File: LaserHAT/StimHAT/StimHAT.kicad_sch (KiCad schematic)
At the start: 120 parts, among them J1 GPIO, J10 OLED 0.91 (GND VCC SCL SDA), J101 ELECTRODE E1/E2, J102 B4B-PH-K-S(LF)(SN), J5 GT-USB-7010ASV, J6 BNC TRIGGER IN, J7 BNC STIM OUT, Q101 MMBT3904, Q102 MMBT3906, Q3 AP30P30Q, Q4 DMMT5401, Q5 AP30P30Q, SW10 MSK12C02, SW6 TS-1088-AR02016, SW7 SKRHADE010, SW9 TS-1088-AR02016, U1 M24C32-WDW6TP, U101 ISO7741FDBQR, U104 TLV76050DBZR, U105 DAC60501ZDGSR, U106 OPA2192IDGKR, U107 CD74HC4053PWR, U108 DG418DY-T1-E3, U109 ISO1640BDR, U110 TLV1702AIDGKR, U4 MCP1700T-3302E/MB, U5 AP2171W, U6 CH340N, U7 MSPM0G3507SRHBR, U8 74LVC2G17GW

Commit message: StimHAT: schematic audit fixes (VREFIO 1 uF, -4.3 V Zener for the 4053's supply margin, 250 mA 0805 inductor code, R113 0603); narrower net classes for routing
Co-Authored-By: Claude Fable 5.1 <noreply@anthropic.com>
Claude-Session: https://claude.ai/code/session_015kiXLxnPpBaXdXJu2EMvn7
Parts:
- C114: value 100nF -> 1uF; LCSC Part # C307331 -> C52923
- D102: value BZT52C4V7S -> BZT52C4V3S; LCSC Part # C353517 -> C22399888
- L101, L102: LCSC Part # C95978 -> C139245
- R113: footprint Resistor_SMD:R_0402_1005Metric -> Resistor_SMD:R_0603_1608Metric; LCSC Part # C25900 -> C23162
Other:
- note added: "(DG418 on, electrode shorted), high -> low. Signals stay within +/-1.25 V; the 4053 runs on +5 / -4.3 V (<= 9.7 V worst case of its 10 V recommended maximum)."
- note added: "clamp each rail to 20 V against GND_ISO (ICs are rated 25 V to their ground). U104: +5V_ISO. R113 / D102: -4.3 V for the 74HC4053."
- note removed: "(DG418 on, electrode shorted), high -> low. Signals stay within +/-1.25 V; the 4053 runs on +5 / -4.7 V (9.7 V of its 10.5 V maximum)."
- note removed: "clamp each rail to 20 V against GND_ISO (ICs are rated 25 V to their ground). U104: +5V_ISO. R113 / D102: -4.7 V for the 74HC4053."
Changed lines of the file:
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@@
     (property "Footprint" "Inductor_SMD:L_0805_2012Metric" (at 238.76 177.8 0) (effects (font (size 1.27 1.27)) (hide yes)))
     (property "Datasheet" "" (at 238.76 177.8 0) (effects (font (size 1.27 1.27)) (hide yes)))
-    (property "LCSC Part #" "C95978" (at 238.76 177.8 0) (effects (font (size 1.27 1.27)) (hide yes)))
+    (property "LCSC Part #" "C139245" (at 238.76 177.8 0) (effects (font (size 1.27 1.27)) (hide yes)))
     (pin "1")
     (pin "2")
@@
     (property "Footprint" "Inductor_SMD:L_0805_2012Metric" (at 238.76 254 0) (effects (font (size 1.27 1.27)) (hide yes)))
     (property "Datasheet" "" (at 238.76 254 0) (effects (font (size 1.27 1.27)) (hide yes)))
-    (property "LCSC Part #" "C95978" (at 238.76 254 0) (effects (font (size 1.27 1.27)) (hide yes)))
+    (property "LCSC Part #" "C139245" (at 238.76 254 0) (effects (font (size 1.27 1.27)) (hide yes)))
     (pin "1")
     (pin "2")
@@
     (property "Reference" "R113" (at 246.38 267.97  0) (effects (font (size 1.27 1.27)) (justify left)))
     (property "Value" "4.7k" (at 246.38 270.51  0) (effects (font (size 1.27 1.27)) (justify left)))
-    (property "Footprint" "Resistor_SMD:R_0402_1005Metric" (at 243.84 269.24 0) (effects (font (size 1.27 1.27)) (hide yes)))
+    (property "Footprint" "Resistor_SMD:R_0603_1608Metric" (at 243.84 269.24 0) (effects (font (size 1.27 1.27)) (hide yes)))
     (property "Datasheet" "" (at 243.84 269.24 0) (effects (font (size 1.27 1.27)) (hide yes)))
-    (property "LCSC Part #" "C25900" (at 243.84 269.24 0) (effects (font (size 1.27 1.27)) (hide yes)))
+    (property "LCSC Part #" "C23162" (at 243.84 269.24 0) (effects (font (size 1.27 1.27)) (hide yes)))
     (pin "1")
     (pin "2")
@@
   (symbol (lib_id "stimhat:D_Zener") (at 259.08 269.24 90) (unit 1) (exclude_from_sim no) (in_bom yes) (on_board yes) (dnp no)
     (property "Reference" "D102" (at 261.62 267.97  90) (effects (font (size 1.27 1.27)) (justify left)))
-    (property "Value" "BZT52C4V7S" (at 261.62 270.51  90) (effects (font (size 1.27 1.27)) (justify left)))
+    (property "Value" "BZT52C4V3S" (at 261.62 270.51  90) (effects (font (size 1.27 1.27)) (justify left)))
     (property "Footprint" "Diode_SMD:D_SOD-323" (at 259.08 269.24 0) (effects (font (size 1.27 1.27)) (hide yes)))
     (property "Datasheet" "" (at 259.08 269.24 0) (effects (font (size 1.27 1.27)) (hide yes)))
-    (property "LCSC Part #" "C353517" (at 259.08 269.24 0) (effects (font (size 1.27 1.27)) (hide yes)))
+    (property "LCSC Part #" "C22399888" (at 259.08 269.24 0) (effects (font (size 1.27 1.27)) (hide yes)))
     (pin "1")
     (pin "2")
@@
   (text "PS1 (hand-fitted) makes +/-15 V from the HAT's 5 V, or J102 brings +/-12..16.8 V from the battery pack (pin 4 = pin 2 = GND_ISO:" (exclude_from_sim no) (at 160.02 276.86 0) (effects (font (size 1.27 1.27)) (justify left bottom)))
   (text "the pack's plug interlock).  L / C filter, then Q101 / Q102 (base 4.7k / 10 uF: ~1.2 V drop, 60 dB ripple rejection above 100 Hz).  D103 / D104" (exclude_from_sim no) (at 160.02 281.94 0) (effects (font (size 1.27 1.27)) (justify left bottom)))
-  (text "clamp each rail to 20 V against GND_ISO (ICs are rated 25 V to their ground).  U104: +5V_ISO.  R113 / D102: -4.7 V for the 74HC4053." (exclude_from_sim no) (at 284.48 172.72 0) (effects (font (size 1.27 1.27)) (justify left bottom)))
+  (text "clamp each rail to 20 V against GND_ISO (ICs are rated 25 V to their ground).  U104: +5V_ISO.  R113 / D102: -4.3 V for the 74HC4053." (exclude_from_sim no) (at 284.48 172.72 0) (effects (font (size 1.27 1.27)) (justify left bottom)))
   (rectangle (start 15.24 289.56) (end 241.3 416.56) (stroke (width 0.2) (type dash)) (fill (type none)))
   (text "6. SET-POINT: DAC60501 (I2C 0x48, 0..1.25 V = VSET_P), U106B INVERTS -> VSET_N, 74HC4053 PICKS SIGN (CATH) AND GATES (EN)" (exclude_from_sim no) (at 16.51 293.37 0) (effects (font (size 2.0 2.0) (bold yes)) (justify left bottom)))
@@
   (symbol (lib_id "stimhat:C") (at 81.28 345.44 0) (unit 1) (exclude_from_sim no) (in_bom yes) (on_board yes) (dnp no)
     (property "Reference" "C114" (at 83.82 344.17  0) (effects (font (size 1.27 1.27)) (justify left)))
-    (property "Value" "100nF" (at 83.82 346.71  0) (effects (font (size 1.27 1.27)) (justify left)))
+    (property "Value" "1uF" (at 83.82 346.71  0) (effects (font (size 1.27 1.27)) (justify left)))
     (property "Footprint" "Capacitor_SMD:C_0402_1005Metric" (at 81.28 345.44 0) (effects (font (size 1.27 1.27)) (hide yes)))
     (property "Datasheet" "" (at 81.28 345.44 0) (effects (font (size 1.27 1.27)) (hide yes)))
-    (property "LCSC Part #" "C307331" (at 81.28 345.44 0) (effects (font (size 1.27 1.27)) (hide yes)))
+    (property "LCSC Part #" "C52923" (at 81.28 345.44 0) (effects (font (size 1.27 1.27)) (hide yes)))
     (pin "1")
     (pin "2")
@@
   )
   (text "Switch 1: CATH picks VSET_P (0) / VSET_N (1) -> SW_P.  Switch 2: EN picks 0 V (0) / SW_P (1) -> V_IN.  Switch 3: RELEASE low -> SHORT_IN high" (exclude_from_sim no) (at 17.78 403.86 0) (effects (font (size 1.27 1.27)) (justify left bottom)))
-  (text "(DG418 on, electrode shorted), high -> low.  Signals stay within +/-1.25 V; the 4053 runs on +5 / -4.7 V (9.7 V of its 10.5 V maximum)." (exclude_from_sim no) (at 17.78 408.94 0) (effects (font (size 1.27 1.27)) (justify left bottom)))
+  (text "(DG418 on, electrode shorted), high -> low.  Signals stay within +/-1.25 V; the 4053 runs on +5 / -4.3 V (<= 9.7 V worst case of its 10 V recommended maximum)." (exclude_from_sim no) (at 17.78 408.94 0) (effects (font (size 1.27 1.27)) (justify left bottom)))
   (text "DAC60501Z: write GAIN (0x04) = 0x0100 first, then DAC (0x08) = code << 4; readback over the same bus.  C115 at U105 VDD, C118 / C119 at U107." (exclude_from_sim no) (at 17.78 414.02 0) (effects (font (size 1.27 1.27)) (justify left bottom)))
   (rectangle (start 248.92 289.56) (end 347.98 391.16) (stroke (width 0.2) (type dash)) (fill (type none)))

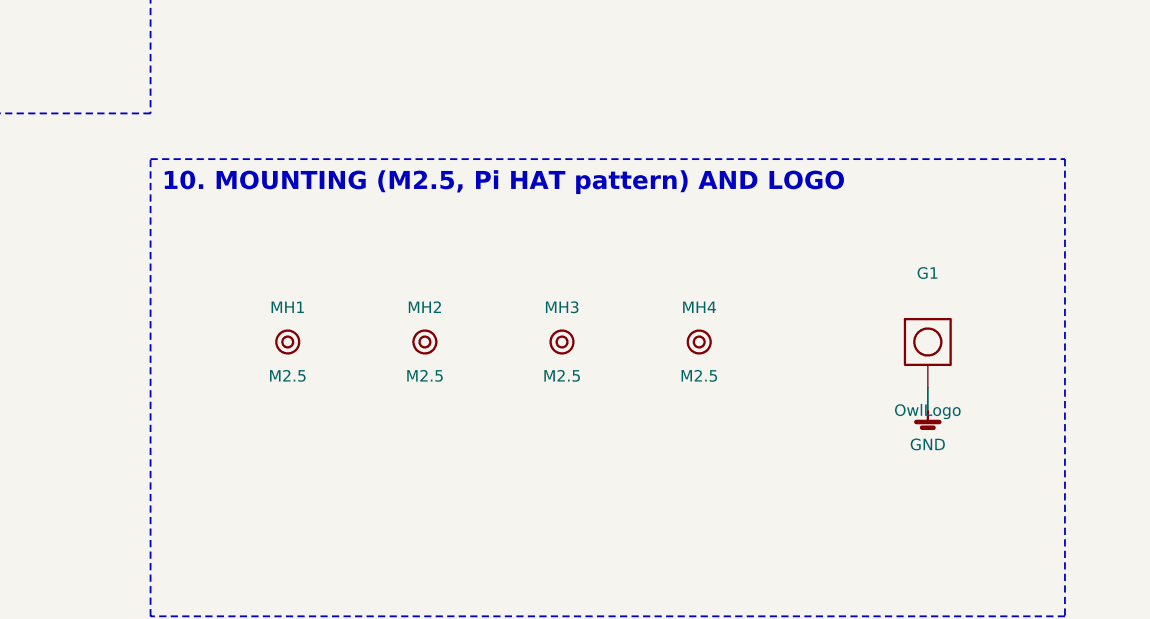
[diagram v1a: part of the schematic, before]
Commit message: StimHAT rev A: routed board (Freerouting + fan-out + SDA_H pre-route), DRC 0/0, fab outputs
Board: placement per floorplan 1g, 2.5 mm isolation barrier as rule areas + .kicad_dru, routed by
tools/autoroute.py (rip -> tools/fanout.py dog-bone fan-out of U7/U101 + GND thermal vias in U7's pad ->
tools/preroute.py locked SDA_H -> Freerouting 500 passes -> trim unused fan-out vias); 0 DRC errors,
0 unconnected, ERC 0/0, path_check and sync_check clean.  Silk of the edge-overhanging connectors
(J6, J7, J101, PS1) stripped from the board copies; joystick footprint loses its silk circle; logo dropped.
fab/StimHAT: gerbers, JLC BOM/CPL, renders.  tools/fixups.py: track/via/silk-strip/maze helpers.

Co-Authored-By: Claude Fable 5.1 <noreply@anthropic.com>
Claude-Session: https://claude.ai/code/session_015kiXLxnPpBaXdXJu2EMvn7
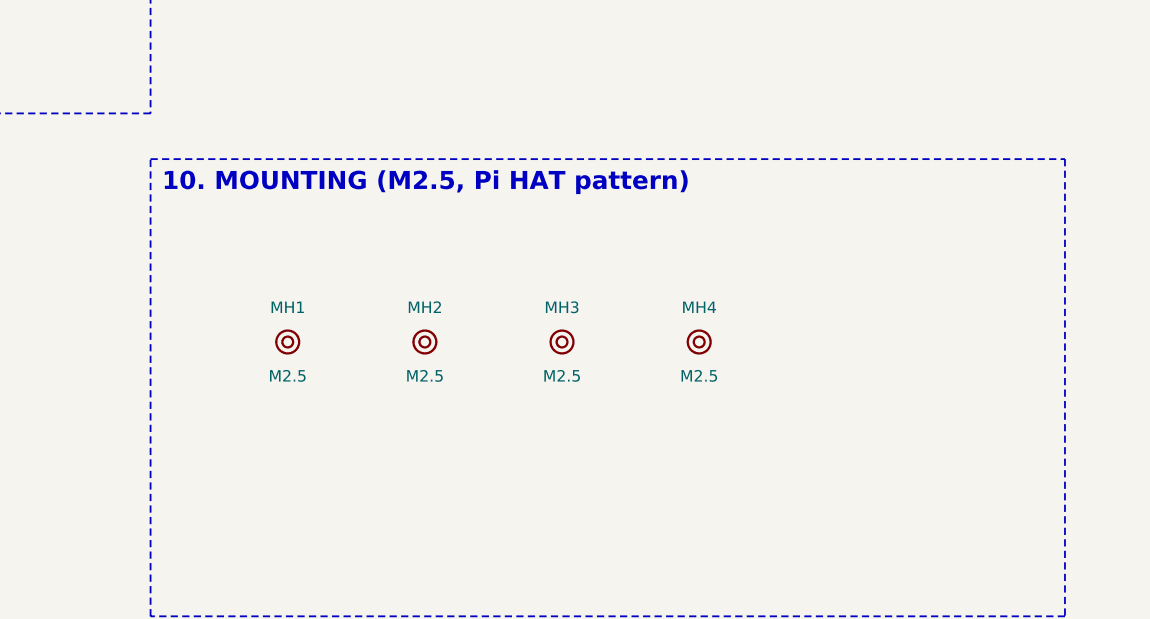
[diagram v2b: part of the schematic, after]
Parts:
- removed G1: OwlLogo, Footprints:OwlLogo_Laser_14mm, symbol stimhat:Logo
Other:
- note added: "10. MOUNTING (M2.5, Pi HAT pattern)"
- note removed: "10. MOUNTING (M2.5, Pi HAT pattern) AND LOGO"
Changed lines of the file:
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@@
   (text "while +5V_ISO is down and when one rail is missing.  R120 / D101 shift the -V-referenced open collectors to 0..5 V." (exclude_from_sim no) (at 358.14 393.7 0) (effects (font (size 1.27 1.27)) (justify left bottom)))
   (rectangle (start 508 162.56) (end 609.6 213.36) (stroke (width 0.2) (type dash)) (fill (type none)))
-  (text "10. MOUNTING (M2.5, Pi HAT pattern) AND LOGO" (exclude_from_sim no) (at 509.27 166.37 0) (effects (font (size 2.0 2.0) (bold yes)) (justify left bottom)))
+  (text "10. MOUNTING (M2.5, Pi HAT pattern)" (exclude_from_sim no) (at 509.27 166.37 0) (effects (font (size 2.0 2.0) (bold yes)) (justify left bottom)))
   (symbol (lib_id "stimhat:MountingHole") (at 523.24 182.88 0) (unit 1) (exclude_from_sim no) (in_bom no) (on_board yes) (dnp no)
     (property "Reference" "MH1" (at 523.24 179.07  0) (effects (font (size 1.27 1.27)) ))
@@
     (property "Datasheet" "" (at 568.96 182.88 0) (effects (font (size 1.27 1.27)) (hide yes)))
     (instances (project "StimHAT" (path "/15556796-a1bc-5b7f-a5a5-0a862d310368" (reference "MH4") (unit 1))))
-  )
-  (symbol (lib_id "stimhat:Logo") (at 594.36 182.88 0) (unit 1) (exclude_from_sim no) (in_bom no) (on_board yes) (dnp no)
-    (property "Reference" "G1" (at 594.36 175.26  0) (effects (font (size 1.27 1.27)) ))
-    (property "Value" "OwlLogo" (at 594.36 190.5  0) (effects (font (size 1.27 1.27)) ))
-    (property "Footprint" "Footprints:OwlLogo_Laser_14mm" (at 594.36 182.88 0) (effects (font (size 1.27 1.27)) (hide yes)))
-    (property "Datasheet" "" (at 594.36 182.88 0) (effects (font (size 1.27 1.27)) (hide yes)))
-    (pin "1")
-    (instances (project "StimHAT" (path "/15556796-a1bc-5b7f-a5a5-0a862d310368" (reference "G1") (unit 1))))
-  )
-  (symbol (lib_id "stimhat:GND") (at 594.36 190.5 0) (unit 1) (exclude_from_sim no) (in_bom no) (on_board no) (dnp no)
-    (property "Reference" "#PWR195" (at 594.36 190.5 0) (effects (font (size 1.27 1.27)) (hide yes)))
-    (property "Value" "GND" (at 594.36 194.31 0) (effects (font (size 1.27 1.27))))
-    (property "Footprint" "" (at 594.36 190.5 0) (effects (font (size 1.27 1.27)) (hide yes)))
-    (property "Datasheet" "" (at 594.36 190.5 0) (effects (font (size 1.27 1.27)) (hide yes)))
-    (pin "1")
-    (instances (project "StimHAT" (path "/15556796-a1bc-5b7f-a5a5-0a862d310368" (reference "#PWR195") (unit 1))))
   )
   (no_connect (at 38.1 68.58))
@@
   (wire (pts (xy 447.04 313.69) (xy 447.04 316.23)) (stroke (width 0) (type default)))
   (wire (pts (xy 482.6 375.92) (xy 482.6 378.46)) (stroke (width 0) (type default)))
-  (wire (pts (xy 594.36 187.96) (xy 594.36 190.5)) (stroke (width 0) (type default)))
   (junction (at 33.02 60.96) (diameter 0) (color 0 0 0 0))
   (junction (at 68.58 60.96) (diameter 0) (color 0 0 0 0))

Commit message: StimHAT rev A: audit fixes (schematic + layout), isolation rule proven live, board finished by hand
Schematic (independent review): CH340N on MSPM0_3V3 (no back-feed into the unpowered MCU), C17 at U6, C18 at
U1, R3 10k, R19/R20 DNP, C125/C126 at the DG418, VREFIO/OA_IN/U5B_IN/OA_OUT labelled, in_bom flags match the
board.  Layout (independent review): the .kicad_dru rules were silently ignored because of their (comment ...)
entries - comments removed, liveness proven with a 25 mm test; three real barrier intrusions fixed (I2C loop above
U109, passage vs strip B pads); standoff keep-outs exclude tracks; decouplers next to their pins; Rails class;
the 0.3 mm +/- rail rule dropped (0.15 class, IPC-2221 B4).  Routing: fan-out + pre-routes (tab, passage, SDA_H)
then Freerouting, the last connections and all DRC fixes by hand (tools/fixups.py).  DRC 0 errors / 0 unconnected,
ERC 0/0, path/sync checks clean; fab outputs regenerated.

Co-Authored-By: Claude Fable 5.1 <noreply@anthropic.com>
Claude-Session: https://claude.ai/code/session_015kiXLxnPpBaXdXJu2EMvn7
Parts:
- added C125, C126: 100nF 50V, Capacitor_SMD:C_0603_1608Metric, symbol stimhat:C
- added C17, C18: 100nF, Capacitor_SMD:C_0402_1005Metric, symbol stimhat:C
- J1, J10, J101, J102, J6, J7, JP1, JP4, JP5, PS1: now left out of the parts list
- R19, R20: now not fitted
- R3: value 47k -> 10k; LCSC Part # C25792 -> C25744
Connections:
- net +3V3: no longer U6.5 (VCC), U6.8 (V3)
- net +3V3_PI: now also C18.1
- net +V_STIM: now also C125.1
- net -V_STIM: now also C126.2
- net GND: now also C17.2, C18.2
- net GND_ISO: now also C125.2, C126.1
- net MSPM0_3V3: now also U6.5 (VCC), U6.8 (V3), C17.1
- net U5B_IN: now reaches R105.2, R106.1, U106.6 (-)
- net OA_OUT: now reaches R115.1, U106.1
- net OA_IN: now reaches C120.1, R114.2, U106.3 (+)
- net VREFIO: now reaches C114.1, U105.10 (VREFIO)

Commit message: StimHAT: second schematic review (no blocker/major): R1/R2 fitted per the HAT guide, R107/R108 2.2k, stale texts, notes
Co-Authored-By: Claude Fable 5.1 <noreply@anthropic.com>
Claude-Session: https://claude.ai/code/session_015kiXLxnPpBaXdXJu2EMvn7
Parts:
- R1, R2: now fitted
- R107, R108: value 4.7k -> 2.2k; LCSC Part # C25900 -> C25879
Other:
- note added: "5. ISOLATED POWER: A0515S (PS1) OR THE BATTERY PACK (J102), LC + CAPACITANCE MULTIPLIERS, CLAMPS, +5 / -4.3 V"
- note added: "Taps at 0.043 x (V+ + |V-|) inside each rail (1.15 V at +/-13.5 V). FAULT_n low while |E1| is past the trip point,"
- note removed: "5. ISOLATED POWER: A0515S (PS1) OR THE BATTERY PACK (J102), LC + CAPACITANCE MULTIPLIERS, CLAMPS, +5 / -4.7 V"
- note removed: "Taps at 0.043 x (V+ + |V-|) inside each rail (0.9 V at +/-13.5 V). FAULT_n low while |E1| is past the trip point,"
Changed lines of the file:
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@@
     (instances (project "StimHAT" (path "/15556796-a1bc-5b7f-a5a5-0a862d310368" (reference "#PWR052") (unit 1))))
   )
-  (symbol (lib_id "stimhat:R") (at 238.76 121.92 0) (unit 1) (exclude_from_sim no) (in_bom yes) (on_board yes) (dnp yes)
+  (symbol (lib_id "stimhat:R") (at 238.76 121.92 0) (unit 1) (exclude_from_sim no) (in_bom yes) (on_board yes) (dnp no)
     (property "Reference" "R1" (at 241.3 120.65  0) (effects (font (size 1.27 1.27)) (justify left)))
     (property "Value" "3.9k" (at 241.3 123.19  0) (effects (font (size 1.27 1.27)) (justify left)))
@@
     (instances (project "StimHAT" (path "/15556796-a1bc-5b7f-a5a5-0a862d310368" (reference "R1") (unit 1))))
   )
-  (symbol (lib_id "stimhat:R") (at 248.92 121.92 0) (unit 1) (exclude_from_sim no) (in_bom yes) (on_board yes) (dnp yes)
+  (symbol (lib_id "stimhat:R") (at 248.92 121.92 0) (unit 1) (exclude_from_sim no) (in_bom yes) (on_board yes) (dnp no)
     (property "Reference" "R2" (at 251.46 120.65  0) (effects (font (size 1.27 1.27)) (justify left)))
     (property "Value" "3.9k" (at 251.46 123.19  0) (effects (font (size 1.27 1.27)) (justify left)))
@@
   (symbol (lib_id "stimhat:R") (at 25.4 213.36 0) (unit 1) (exclude_from_sim no) (in_bom yes) (on_board yes) (dnp no)
     (property "Reference" "R107" (at 27.94 212.09  0) (effects (font (size 1.27 1.27)) (justify left)))
-    (property "Value" "4.7k" (at 27.94 214.63  0) (effects (font (size 1.27 1.27)) (justify left)))
+    (property "Value" "2.2k" (at 27.94 214.63  0) (effects (font (size 1.27 1.27)) (justify left)))
     (property "Footprint" "Resistor_SMD:R_0402_1005Metric" (at 25.4 213.36 0) (effects (font (size 1.27 1.27)) (hide yes)))
     (property "Datasheet" "" (at 25.4 213.36 0) (effects (font (size 1.27 1.27)) (hide yes)))
-    (property "LCSC Part #" "C25900" (at 25.4 213.36 0) (effects (font (size 1.27 1.27)) (hide yes)))
+    (property "LCSC Part #" "C25879" (at 25.4 213.36 0) (effects (font (size 1.27 1.27)) (hide yes)))
     (pin "1")
     (pin "2")
@@
   (symbol (lib_id "stimhat:R") (at 35.56 213.36 0) (unit 1) (exclude_from_sim no) (in_bom yes) (on_board yes) (dnp no)
     (property "Reference" "R108" (at 38.1 212.09  0) (effects (font (size 1.27 1.27)) (justify left)))
-    (property "Value" "4.7k" (at 38.1 214.63  0) (effects (font (size 1.27 1.27)) (justify left)))
+    (property "Value" "2.2k" (at 38.1 214.63  0) (effects (font (size 1.27 1.27)) (justify left)))
     (property "Footprint" "Resistor_SMD:R_0402_1005Metric" (at 35.56 213.36 0) (effects (font (size 1.27 1.27)) (hide yes)))
     (property "Datasheet" "" (at 35.56 213.36 0) (effects (font (size 1.27 1.27)) (hide yes)))
-    (property "LCSC Part #" "C25900" (at 35.56 213.36 0) (effects (font (size 1.27 1.27)) (hide yes)))
+    (property "LCSC Part #" "C25879" (at 35.56 213.36 0) (effects (font (size 1.27 1.27)) (hide yes)))
     (pin "1")
     (pin "2")
@@
   (text "and R109 / R110 are the I2C pull-ups.  ISO1640: side 1 (pins 1-4) = MCU side, side 2 = DAC side.  C101 at U101.1, C103 at U109.1." (exclude_from_sim no) (at 17.78 276.86 0) (effects (font (size 1.27 1.27)) (justify left bottom)))
   (rectangle (start 157.48 162.56) (end 355.6 284.48) (stroke (width 0.2) (type dash)) (fill (type none)))
-  (text "5. ISOLATED POWER: A0515S (PS1) OR THE BATTERY PACK (J102), LC + CAPACITANCE MULTIPLIERS, CLAMPS, +5 / -4.7 V" (exclude_from_sim no) (at 158.75 166.37 0) (effects (font (size 2.0 2.0) (bold yes)) (justify left bottom)))
+  (text "5. ISOLATED POWER: A0515S (PS1) OR THE BATTERY PACK (J102), LC + CAPACITANCE MULTIPLIERS, CLAMPS, +5 / -4.3 V" (exclude_from_sim no) (at 158.75 166.37 0) (effects (font (size 2.0 2.0) (bold yes)) (justify left bottom)))
   (symbol (lib_id "stimhat:A0515S") (at 187.96 182.88 0) (unit 1) (exclude_from_sim no) (in_bom no) (on_board yes) (dnp yes)
     (property "Reference" "PS1" (at 187.96 173.99  0) (effects (font (size 1.27 1.27)) ))
@@
     (instances (project "StimHAT" (path "/15556796-a1bc-5b7f-a5a5-0a862d310368" (reference "#PWR202") (unit 1))))
   )
-  (text "Taps at 0.043 x (V+ + |V-|) inside each rail (0.9 V at +/-13.5 V).  FAULT_n low while |E1| is past the trip point," (exclude_from_sim no) (at 358.14 388.62 0) (effects (font (size 1.27 1.27)) (justify left bottom)))
+  (text "Taps at 0.043 x (V+ + |V-|) inside each rail (1.15 V at +/-13.5 V).  FAULT_n low while |E1| is past the trip point," (exclude_from_sim no) (at 358.14 388.62 0) (effects (font (size 1.27 1.27)) (justify left bottom)))
   (text "while +5V_ISO is down and when one rail is missing.  R120 / D101 shift the -V-referenced open collectors to 0..5 V." (exclude_from_sim no) (at 358.14 393.7 0) (effects (font (size 1.27 1.27)) (justify left bottom)))
   (rectangle (start 508 162.56) (end 609.6 213.36) (stroke (width 0.2) (type dash)) (fill (type none)))

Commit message: StimHAT: second layout review - DC-DC body under the tab (mirrored footprint), J101 between PS1's pads, 0.3 mm rule for the hand-soldered connector pads, tab re-threaded, labels fixed
Co-Authored-By: Claude Fable 5.1 <noreply@anthropic.com>
Claude-Session: https://claude.ai/code/session_015kiXLxnPpBaXdXJu2EMvn7
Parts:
- PS1: footprint estim:DCDC_SIP6_A0515S -> stimhat:DCDC_SIP6_A0515S_BodyN
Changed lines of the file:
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@@
     (property "Reference" "PS1" (at 187.96 173.99  0) (effects (font (size 1.27 1.27)) ))
     (property "Value" "A0515S-1WR3" (at 187.96 191.77  0) (effects (font (size 1.27 1.27)) ))
-    (property "Footprint" "estim:DCDC_SIP6_A0515S" (at 187.96 182.88 0) (effects (font (size 1.27 1.27)) (hide yes)))
+    (property "Footprint" "stimhat:DCDC_SIP6_A0515S_BodyN" (at 187.96 182.88 0) (effects (font (size 1.27 1.27)) (hide yes)))
     (property "Datasheet" "" (at 187.96 182.88 0) (effects (font (size 1.27 1.27)) (hide yes)))
     (pin "1")
